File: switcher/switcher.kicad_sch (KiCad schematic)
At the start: 37 parts, among them J2 Conn_01x18, J3_LED1 Conn_02x08_Odd_Even, K0 HFD2_005-S-L2-D, K1 HFD2_005-S-L2-D, K2 HFD2_005-S-L2-D, U1 INA3221_Module, U2 ULN2803A, U3 ULN2803A, U5 MCP2551-I-P, U6 ChinaBluePill-bluepill-D3_Boa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

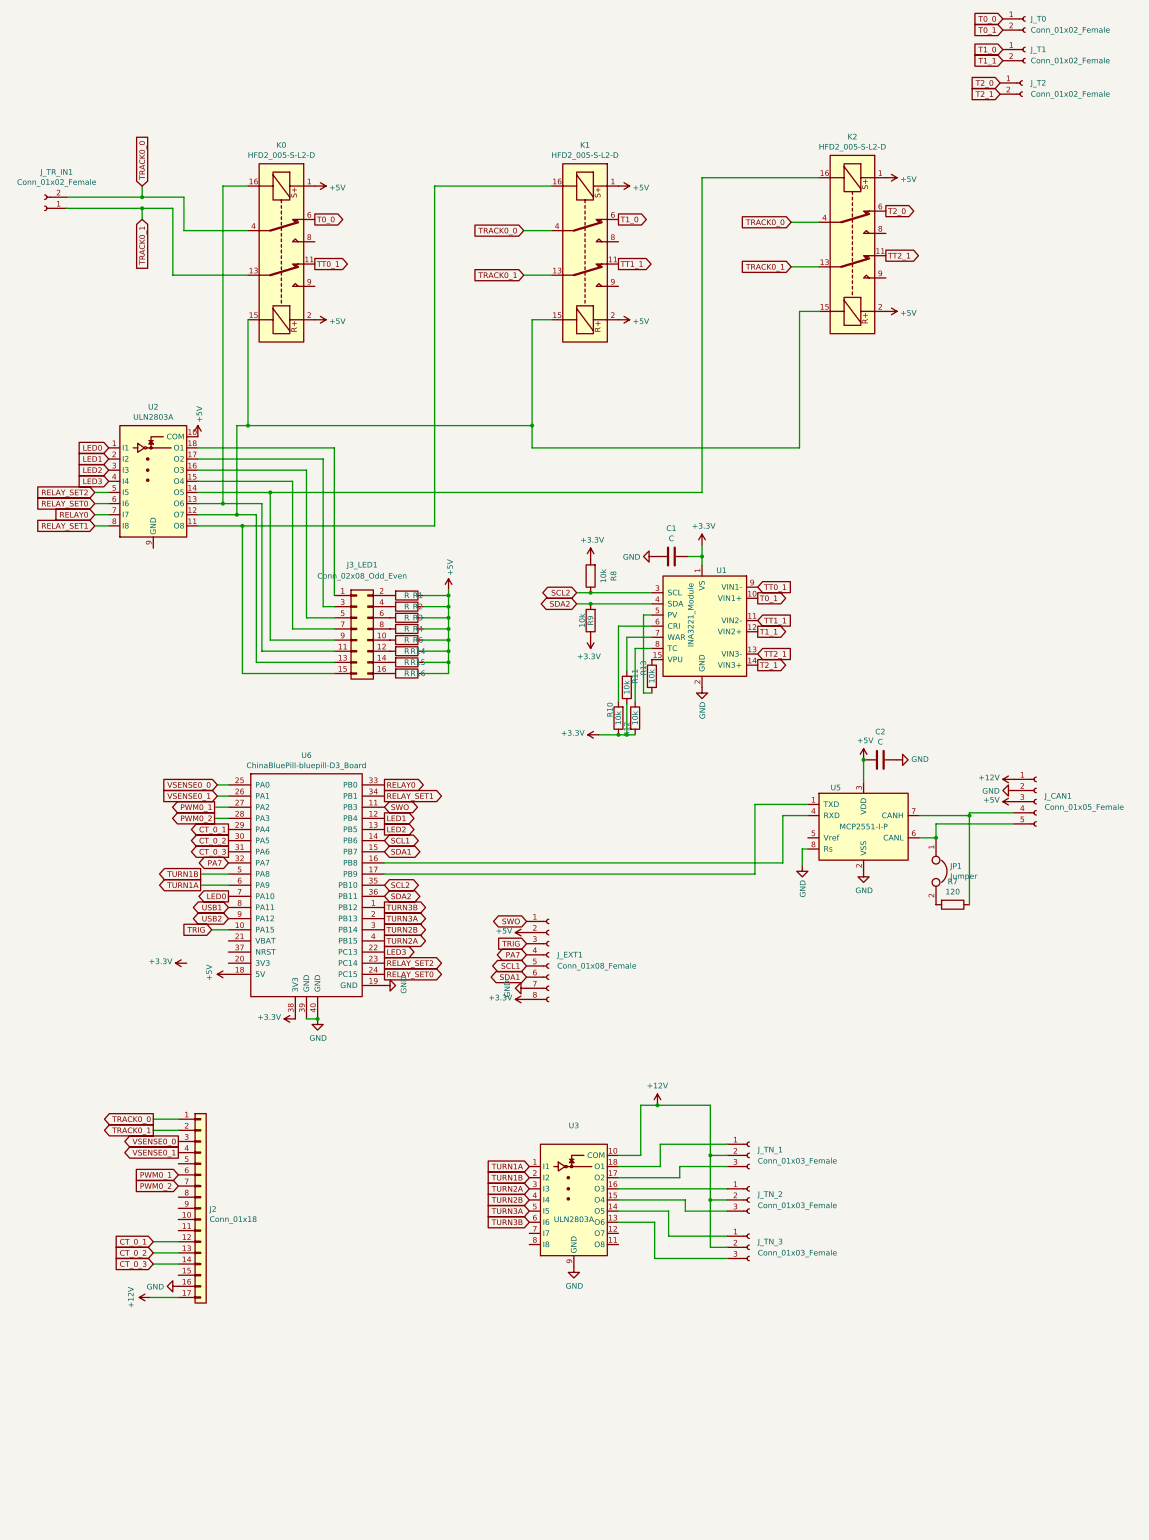
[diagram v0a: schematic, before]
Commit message: add switcher board, derived from dispatcher
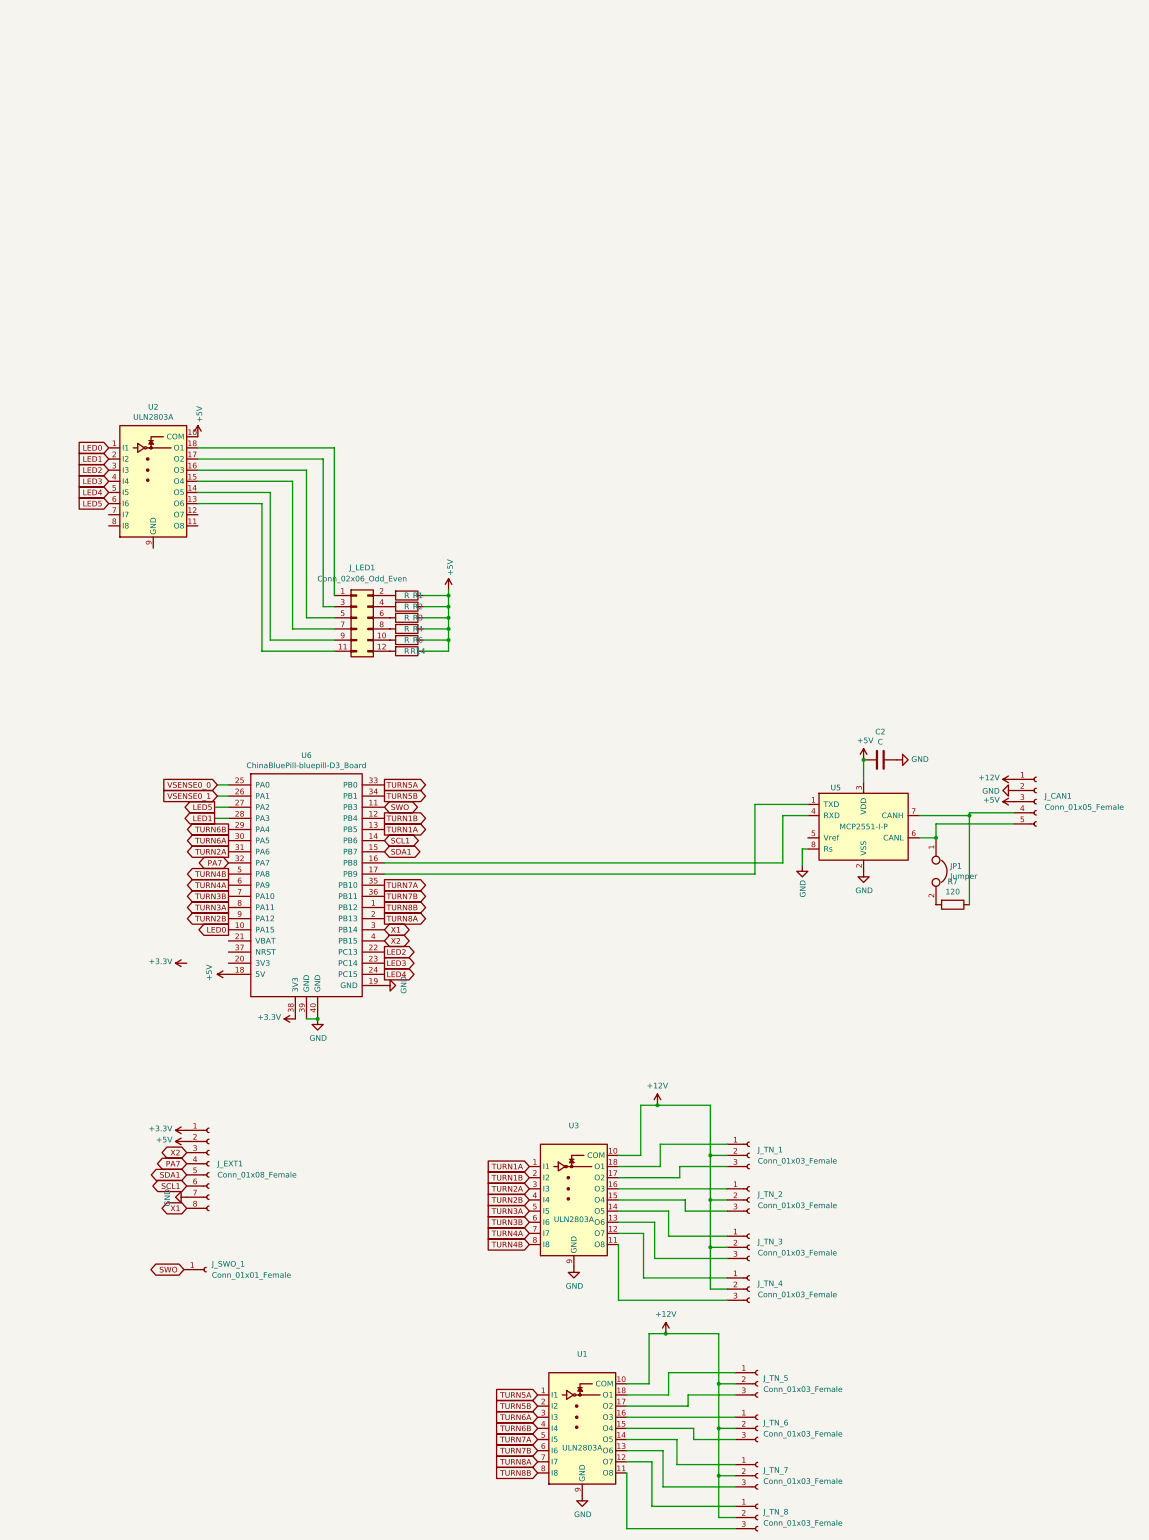
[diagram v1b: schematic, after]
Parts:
- removed C1: C, Capacitor_THT:C_Disc_D3.4mm_W2.1mm_P2.50mm, symbol Device:C
- removed J2: Conn_01x18, Connector_PinHeader_2.54mm:PinHeader_1x17_P2.54mm_Vertical, symbol Connector_Generic:Conn_01x17
- removed J3_LED1: Conn_02x08_Odd_Even, Connector_PinHeader_2.54mm:PinHeader_2x08_P2.54mm_Vertical, symbol Connector_Generic:Conn_02x08_Odd_Even
- removed J_T0, J_T1, J_T2, J_TR_IN1: Conn_01x02_Female, Connector_PinHeader_2.54mm:PinHeader_1x02_P2.54mm_Vertical, symbol Connector:Conn_01x02_Female
- removed K0, K1, K2: HFD2_005-S-L2-D, Modules:HFD2-005-S-L2-D, symbol VadimNsk:HFD2_005-S-L2-D
- removed R10, R11, R12, R13, R8, R9: 10k, Resistor_THT:R_Axial_DIN0207_L6.3mm_D2.5mm_P7.62mm_Horizontal, symbol Device:R
- removed R15, R16: R, Resistor_THT:R_Axial_DIN0207_L6.3mm_D2.5mm_P7.62mm_Horizontal, symbol Device:R
- removed U1: INA3221_Module, jwm_kicad_footprints_misc:INA3221_Module, symbol jwm_kicad_symbols_misc:INA3221_Module
- added J_LED1: Conn_02x06_Odd_Even, Connector_PinHeader_2.54mm:PinHeader_2x06_P2.54mm_Vertical, symbol Connector_Generic:Conn_02x06_Odd_Even
- added J_SWO_1: Conn_01x01_Female, Connector_PinHeader_2.54mm:PinHeader_1x01_P2.54mm_Vertical, symbol Connector:Conn_01x01_Female
- added J_TN_4, J_TN_5, J_TN_6, J_TN_7, J_TN_8: Conn_01x03_Female, Connector_PinHeader_2.54mm:PinHeader_1x03_P2.54mm_Vertical, symbol Connector:Conn_01x03_Female
- added U1: ULN2803A, Package_DIP:DIP-18_W7.62mm, symbol Transistor_Array:ULN2803A
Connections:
- net CT_0_3 is gone; now on net TURN2A: U6.31 (PA6)
- net PWM0_2 is gone; now on net LED1: U6.28 (PA3)
- net USB1 is gone; now on net TURN3A: U6.8 (PA11)
- net USB2 is gone; now on net TURN2B: U6.9 (PA12)
- net +12V: now also J_TN_4.2 (Pin_2), J_TN_5.2 (Pin_2), J_TN_6.2 (Pin_2), J_TN_7.2 (Pin_2), J_TN_8.2 (Pin_2), U1.10 (COM)
- net +3V3: now also J_EXT1.1 (Pin_1); no longer J_EXT1.8 (Pin_8)
- net GND: now also U1.9 (GND)
- net LED0: now also U6.10 (PA15); no longer U6.7 (PA10)
- net LED1: no longer U6.12 (PB4)
- net LED2: now also U6.22 (PC13); no longer U6.13 (PB5)
- net LED3: now also U6.23 (PC14); no longer U6.22 (PC13)
- net SCL1: now also J_EXT1.6 (Pin_6); no longer J_EXT1.5 (Pin_5)
- net SDA1: now also J_EXT1.5 (Pin_5); no longer J_EXT1.6 (Pin_6)
- net SWO: now also J_SWO_1.1 (Pin_1); no longer J_EXT1.1 (Pin_1)
- net TURN1A: now also U6.13 (PB5); no longer U6.6 (PA9)
- net TURN1B: now also U6.12 (PB4); no longer U6.5 (PA8)
- net TURN2A: no longer U6.4 (PB15)
- net TURN2B: no longer U6.3 (PB14)
- net TURN3A: no longer U6.2 (PB13)
- net TURN3B: now also U6.7 (PA10); no longer U6.1 (PB12)
- net at U2.13 (O6): now also J_LED1.11 (Pin_11)
- net at U2.14 (O5): now also J_LED1.9 (Pin_9)
- net at U2.15 (O4): now also J_LED1.7 (Pin_7)
- net at U2.16 (O3): now also J_LED1.5 (Pin_5)
- net at U2.17 (O2): now also J_LED1.3 (Pin_3)
- net at U2.18 (O1): now also J_LED1.1 (Pin_1)
- net at U3.11 (O8): now also J_TN_4.3 (Pin_3)
- net at U3.12 (O7): now also J_TN_4.1 (Pin_1)
- net TURN4A: now reaches U3.7 (I7)
- net TURN4A: now also U6.6 (PA9)
- net TURN4B: now reaches U3.8 (I8)
- net TURN4B: now also U6.5 (PA8)
- net at R6.2: now also J_LED1.10 (Pin_10)
- net at R14.2: now also J_LED1.12 (Pin_12)
- net at R1.2: now also J_LED1.2 (Pin_2)
- net at R2.2: now also J_LED1.4 (Pin_4)
- net at R3.2: now also J_LED1.6 (Pin_6)
- net at R4.2: now also J_LED1.8 (Pin_8)
- net CT_0_1 renamed TURN6B
- net TURN6B: now also U1.4 (I4)
- net CT_0_2 renamed TURN6A
- net TURN6A: now also U1.3 (I3)
- net PWM0_1 renamed LED5
- net LED5: now also U2.6 (I6)
- net RELAY0: no longer names the net of U2.7 (I7)
- net RELAY0: no longer U6.33 (PB0)
- net RELAY_SET0 renamed LED4
- net LED4: now also U2.5 (I5); no longer U2.6 (I6)
- net RELAY_SET1: no longer names the net of U2.8 (I8)
- net RELAY_SET1: no longer U6.34 (PB1)
- removed net RELAY_SET2: U2.5 (I5), U6.23 (PC14)
- net SCL2 renamed TURN7A
- net TURN7A: now also U1.5 (I5)
- net SDA2 renamed TURN7B
- net TURN7B: now also U1.6 (I6)
- net TRIG renamed X2
- net X2: now also U6.4 (PB15); no longer U6.10 (PA15)
- new net: J_TN_8.1 (Pin_1), U1.12 (O7)
- new net: J_TN_8.3 (Pin_3), U1.11 (O8)
- new net: J_TN_5.1 (Pin_1), U1.18 (O1)
- new net: J_TN_5.3 (Pin_3), U1.17 (O2)
- new net: J_TN_6.1 (Pin_1), U1.16 (O3)
- new net: J_TN_6.3 (Pin_3), U1.15 (O4)
- new net: J_TN_7.3 (Pin_3), U1.13 (O6)
- new net: J_TN_7.1 (Pin_1), U1.14 (O5)
- new net TURN5A: U1.1 (I1), U6.33 (PB0)
- new net TURN5B: U1.2 (I2), U6.34 (PB1)
- new net TURN8A: U1.7 (I7), U6.2 (PB13)
- new net TURN8B: U1.8 (I8), U6.1 (PB12)
- new net X1: J_EXT1.8 (Pin_8), U6.3 (PB14)
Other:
- moved on the sheet: J_EXT1

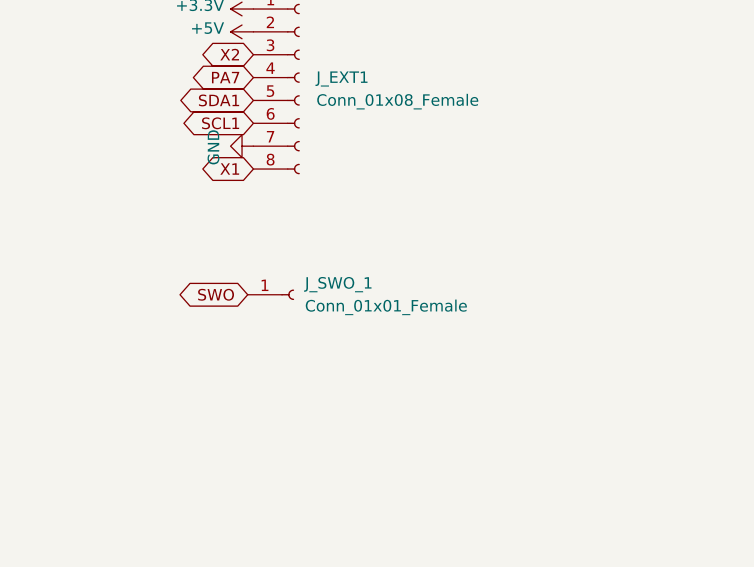
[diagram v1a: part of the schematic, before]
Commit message: update switcher board, DRC OK
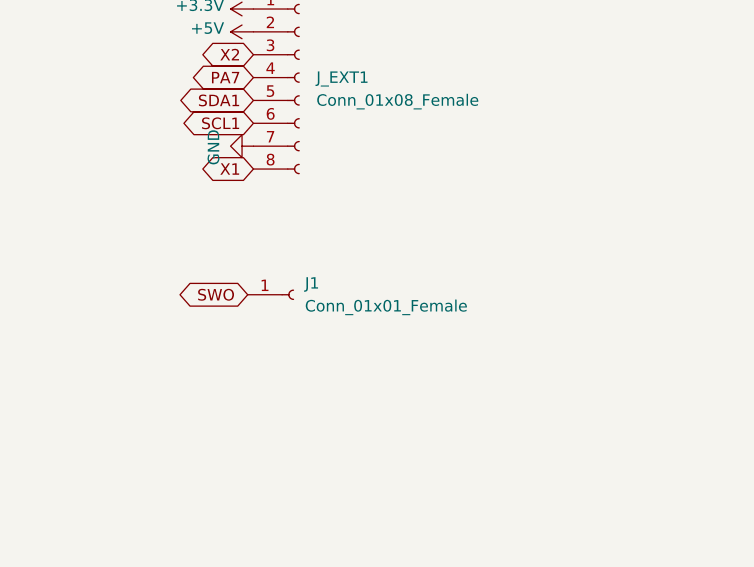
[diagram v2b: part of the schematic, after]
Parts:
- renumbered J_SWO_1 to J1
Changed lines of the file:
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@@
   (symbol (lib_id "Connector:Conn_01x01_Female") (at 80.01 304.8 0) (unit 1)
     (in_bom yes) (on_board yes) (fields_autoplaced)
-    (property "Reference" "J_SWO_1" (id 0) (at 81.28 303.5299 0)
+    (property "Reference" "J1" (id 0) (at 81.28 303.5299 0)
       (effects (font (size 1.27 1.27)) (justify left))
     )
@@
       (reference "C2") (unit 1) (value "C") (footprint "Capacitor_THT:C_Disc_D3.4mm_W2.1mm_P2.50mm")
     )
+    (path "/48132d4a-2aa0-40cd-8961-8e534a6db5ff"
+      (reference "J1") (unit 1) (value "Conn_01x01_Female") (footprint "Connector_PinHeader_2.54mm:PinHeader_1x01_P2.54mm_Vertical")
+    )
     (path "/00000000-0000-0000-0000-000061b26290"
       (reference "JP1") (unit 1) (value "Jumper") (footprint "Connector_PinHeader_2.54mm:PinHeader_1x02_P2.54mm_Vertical")
@@
       (reference "J_LED1") (unit 1) (value "Conn_02x06_Odd_Even") (footprint "Connector_PinHeader_2.54mm:PinHeader_2x06_P2.54mm_Vertical")
     )
-    (path "/48132d4a-2aa0-40cd-8961-8e534a6db5ff"
-      (reference "J_SWO_1") (unit 1) (value "Conn_01x01_Female") (footprint "Connector_PinHeader_2.54mm:PinHeader_1x01_P2.54mm_Vertical")
-    )
     (path "/d9c7d2fa-331e-4a7d-a954-b103d65a28a6"
